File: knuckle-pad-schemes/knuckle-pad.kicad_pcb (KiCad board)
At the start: 2 copper layers, 127.6 x 115.3 mm, 67 parts, among them SW1 SW_Push, SW10 SW_Push, SW11 SW_Push, SW12 SW_Push, SW13 SW_Push, SW14 SW_Push, SW15 SW_Push, SW16 SW_Push, SW17 SW_Push, SW18 SW_Push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

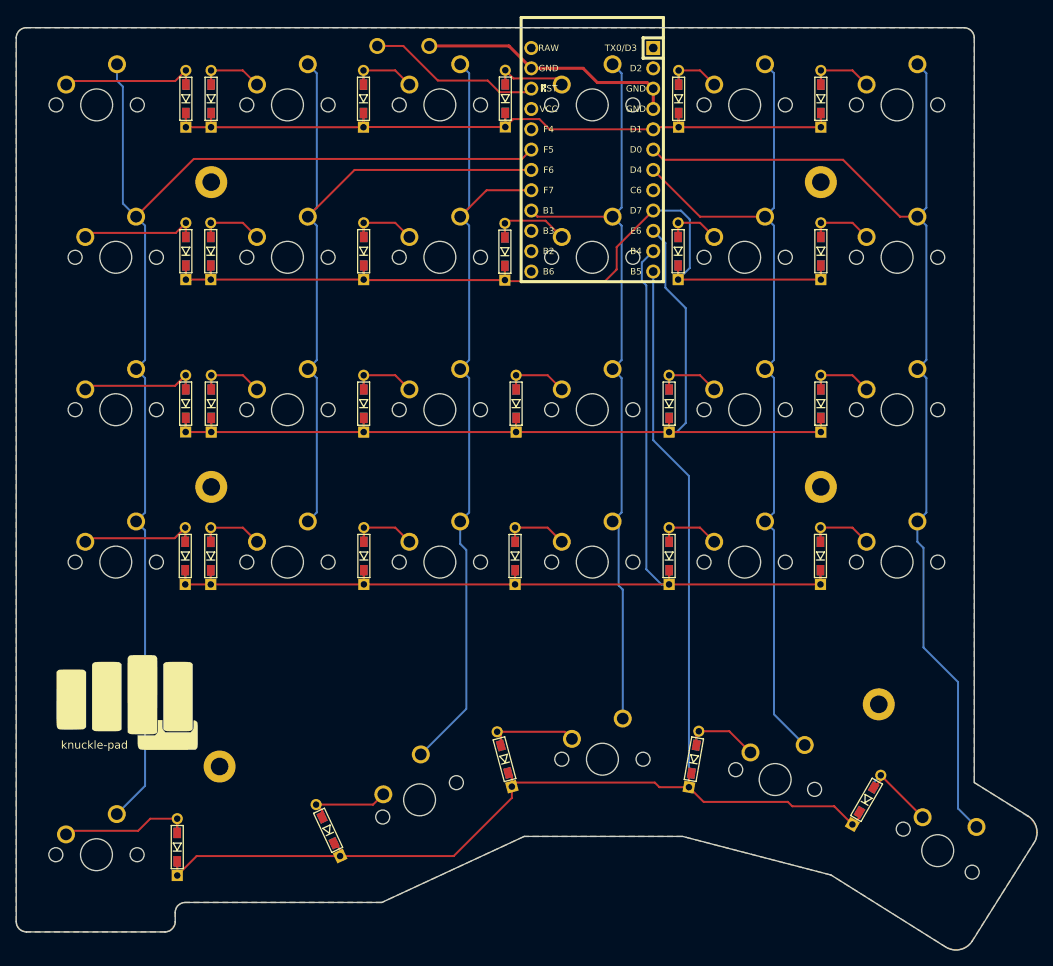
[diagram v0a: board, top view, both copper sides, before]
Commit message: changed mounting hole pos to match plate
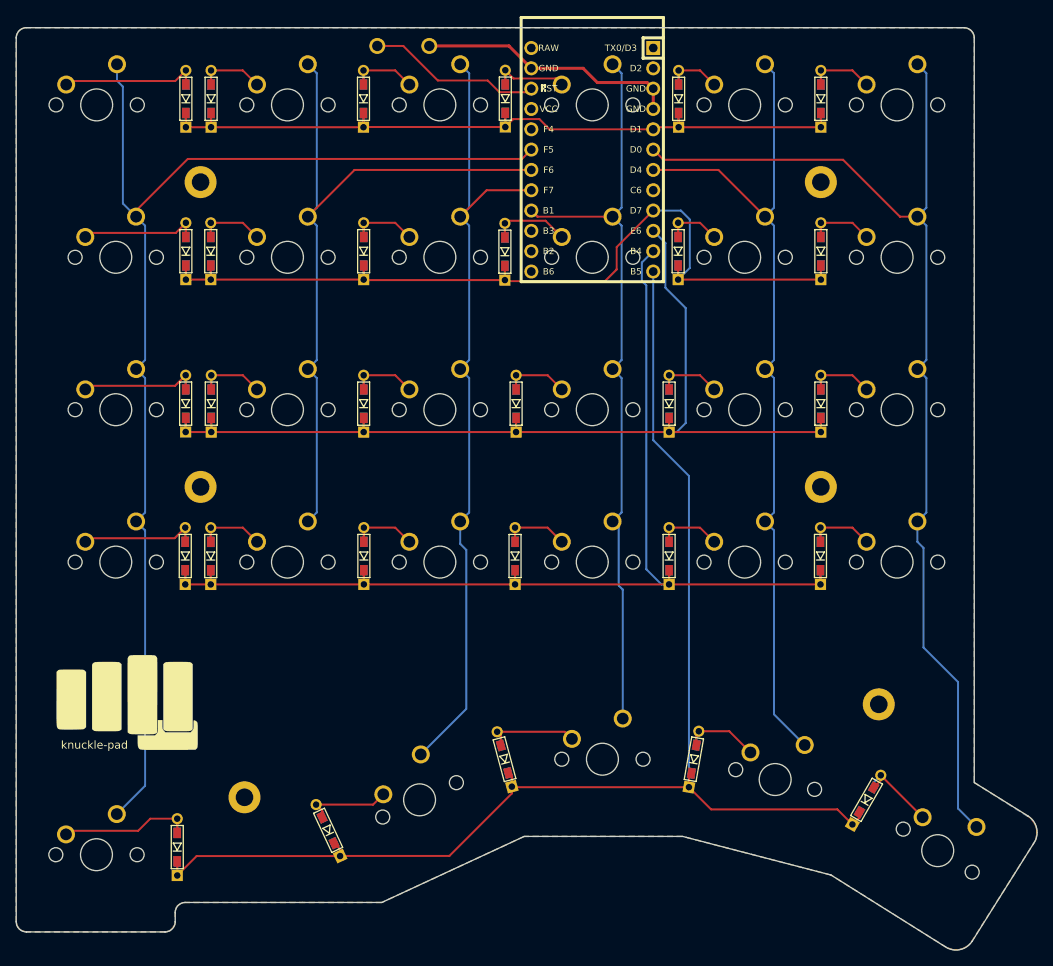
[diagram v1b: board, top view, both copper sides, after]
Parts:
- moved H3 4.95 mm to (109.4, 130.0)
- moved H2 1.33 mm to (103.9, 53.1)
- moved H4 1.33 mm to (103.9, 91.2)
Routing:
- net row4: track 177.3 -> 176.5 mm
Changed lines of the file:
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@@
     (thickness 1.6)
     (drawings 22)
-    (tracks 373)
+    (tracks 372)
     (zones 0)
     (modules 67)
@@
   )
   (module used_footprints:M2_HOLE_PCB (layer F.Cu)
-    (at 105.283 91.186)
+    (at 103.9495 91.186)
     (fp_text reference H4 (at 0 2.7) (layer F.SilkS) hide
       (effects (font (size 1 1) (thickness 0.15)))
@@
   )
   (module used_footprints:M2_HOLE_PCB (layer F.Cu)
-    (at 106.3244 126.1364)
+    (at 109.4359 129.9845)
     (fp_text reference H3 (at 0 2.7) (layer F.SilkS) hide
       (effects (font (size 1 1) (thickness 0.15)))
@@
   )
   (module used_footprints:M2_HOLE_PCB (layer F.Cu)
-    (at 105.283 53.086)
+    (at 103.9495 53.086)
     (fp_text reference H2 (at 0 2.7) (layer F.SilkS) hide
       (effects (font (size 1 1) (thickness 0.15)))
@@
   (segment (start 186.3105 132.48889) (end 185.423 133.37639) (width 0.25) (layer F.Cu) (net 13))
   (segment (start 186.3105 131.839195) (end 186.3105 132.48889) (width 0.25) (layer F.Cu) (net 13))
-  (segment (start 183.15297 131.10636) (end 177.90586 131.10636) (width 0.25) (layer F.Cu) (net 13))
-  (segment (start 185.423 133.37639) (end 183.15297 131.10636) (width 0.25) (layer F.Cu) (net 13))
-  (segment (start 177.90586 131.10636) (end 177.3555 130.556) (width 0.25) (layer F.Cu) (net 13))
-  (segment (start 166.829481 130.556) (end 164.991549 128.718068) (width 0.25) (layer F.Cu) (net 13))
-  (segment (start 177.3555 130.556) (end 166.829481 130.556) (width 0.25) (layer F.Cu) (net 13))
-  (segment (start 164.991549 128.718068) (end 161.293568 128.718068) (width 0.25) (layer F.Cu) (net 13))
-  (segment (start 161.293568 128.718068) (end 160.7185 128.143) (width 0.25) (layer F.Cu) (net 13))
-  (segment (start 143.364249 128.143) (end 142.856212 128.651037) (width 0.25) (layer F.Cu) (net 13))
-  (segment (start 160.7185 128.143) (end 143.364249 128.143) (width 0.25) (layer F.Cu) (net 13))
   (segment (start 164.991549 127.278259) (end 165.299774 126.970034) (width 0.25) (layer F.Cu) (net 13))
   (segment (start 164.991549 128.718068) (end 164.991549 127.278259) (width 0.25) (layer F.Cu) (net 13))
   (segment (start 142.856212 127.395922) (end 142.396808 126.936518) (width 0.25) (layer F.Cu) (net 13))
   (segment (start 142.856212 128.651037) (end 142.856212 127.395922) (width 0.25) (layer F.Cu) (net 13))
-  (segment (start 142.856212 128.651037) (end 142.856212 130.066788) (width 0.25) (layer F.Cu) (net 13))
-  (segment (start 135.593607 137.329393) (end 121.388295 137.329393) (width 0.25) (layer F.Cu) (net 13))
-  (segment (start 142.856212 130.066788) (end 135.593607 137.329393) (width 0.25) (layer F.Cu) (net 13))
   (segment (start 121.388295 136.470844) (end 120.638147 135.720696) (width 0.25) (layer F.Cu) (net 13))
   (segment (start 121.388295 137.329393) (end 121.388295 136.470844) (width 0.25) (layer F.Cu) (net 13))
@@
   (segment (start 164.991549 89.807549) (end 160.528 85.344) (width 0.25) (layer B.Cu) (net 13))
   (segment (start 164.991549 128.718068) (end 164.991549 89.807549) (width 0.25) (layer B.Cu) (net 13))
+  (segment (start 142.923243 128.718068) (end 142.856212 128.651037) (width 0.25) (layer F.Cu) (net 13))
+  (segment (start 164.991549 128.718068) (end 142.923243 128.718068) (width 0.25) (layer F.Cu) (net 13))
+  (segment (start 121.405288 137.3124) (end 121.388295 137.329393) (width 0.25) (layer F.Cu) (net 13))
+  (segment (start 135.0518 137.3124) (end 121.405288 137.3124) (width 0.25) (layer F.Cu) (net 13))
+  (segment (start 142.856212 129.507988) (end 135.0518 137.3124) (width 0.25) (layer F.Cu) (net 13))
+  (segment (start 142.856212 128.651037) (end 142.856212 129.507988) (width 0.25) (layer F.Cu) (net 13))
+  (segment (start 167.769281 131.4958) (end 164.991549 128.718068) (width 0.25) (layer F.Cu) (net 13))
+  (segment (start 183.54241 131.4958) (end 167.769281 131.4958) (width 0.25) (layer F.Cu) (net 13))
+  (segment (start 185.423 133.37639) (end 183.54241 131.4958) (width 0.25) (layer F.Cu) (net 13))
   (segment (start 101.0285 134.4325) (end 101.0285 132.6575) (width 0.25) (layer F.Cu) (net 14))
   (segment (start 101.0285 132.6575) (end 97.657 132.6575) (width 0.25) (layer F.Cu) (net 14))
@@
   (segment (start 95.885 95.504) (end 97.009999 96.628999) (width 0.25) (layer B.Cu) (net 39))
   (segment (start 144.1196 50.1904) (end 145.288 49.022) (width 0.25) (layer F.Cu) (net 39))
-  (segment (start 103.0986 50.1904) (end 144.1196 50.1904) (width 0.25) (layer F.Cu) (net 39))
-  (segment (start 95.885 57.404) (end 103.0986 50.1904) (width 0.25) (layer F.Cu) (net 39))
+  (segment (start 102.3493 50.1904) (end 144.1196 50.1904) (width 0.25) (layer F.Cu) (net 39))
+  (segment (start 95.885 56.6547) (end 102.3493 50.1904) (width 0.25) (layer F.Cu) (net 39))
+  (segment (start 95.885 57.404) (end 95.885 56.6547) (width 0.25) (layer F.Cu) (net 39))
   (segment (start 118.472999 56.279001) (end 117.348 57.404) (width 0.25) (layer B.Cu) (net 40))
   (segment (start 118.472999 39.478999) (end 118.472999 56.279001) (width 0.25) (layer B.Cu) (net 40))
@@
   (segment (start 175.622999 96.628999) (end 175.622999 119.608864) (width 0.25) (layer B.Cu) (net 43))
   (segment (start 174.498 95.504) (end 175.622999 96.628999) (width 0.25) (layer B.Cu) (net 43))
-  (segment (start 166.37 57.404) (end 160.528 51.562) (width 0.25) (layer F.Cu) (net 43))
-  (segment (start 174.498 57.404) (end 166.37 57.404) (width 0.25) (layer F.Cu) (net 43))
+  (segment (start 168.6687 51.562) (end 160.528 51.562) (width 0.25) (layer F.Cu) (net 43))
+  (segment (start 174.498 57.3913) (end 168.6687 51.562) (width 0.25) (layer F.Cu) (net 43))
+  (segment (start 174.498 57.404) (end 174.498 57.3913) (width 0.25) (layer F.Cu) (net 43))
   (segment (start 194.31 75.692) (end 193.548 76.454) (width 0.25) (layer B.Cu) (net 44))
   (segment (start 194.31 94.742) (end 193.548 95.504) (width 0.25) (layer B.Cu) (net 44))

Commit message: clean up
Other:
- board size 127.6 x 115.3 mm -> 127.2 x 115.3 mm
- board text added: "designed by /github.com/tileissner"
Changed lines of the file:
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@@
   (general
     (thickness 1.6)
-    (drawings 22)
+    (drawings 23)
     (tracks 372)
     (zones 0)
@@
     )
   )
-  (gr_text knuckle-pad (at 90.678 123.444) (layer F.SilkS)
-    (effects (font (size 1 1) (thickness 0.15)))
+  (gr_text "designed by /github.com/tileissner" (at 94.6912 124.64034) (layer F.SilkS)
+    (effects (font (size 0.5842 0.6477) (thickness 0.0762)))
+  )
+  (gr_arc (start 82.5754 35.052) (end 82.5754 33.782) (angle -90) (layer Edge.Cuts) (width 0.05))
+  (gr_arc (start 82.5754 145.542) (end 81.3054 145.542) (angle -90) (layer Edge.Cuts) (width 0.05))
+  (gr_text knuckle-pad (at 90.8558 123.00712) (layer F.SilkS)
+    (effects (font (size 1.0414 1.0414) (thickness 0.13335)))
   )
   (gr_arc (start 206.121001 134.365999) (end 207.391 132.334) (angle 93.53229458) (layer Edge.Cuts) (width 0.05))
   (gr_arc (start 198.374001 146.685001) (end 200.406 147.955) (angle 93.53229458) (layer Edge.Cuts) (width 0.05))
   (gr_line (start 200.66 35.052) (end 200.66 128.143) (layer Edge.Cuts) (width 0.05))
-  (gr_line (start 82.169 33.782) (end 199.39 33.782) (layer Edge.Cuts) (width 0.05))
-  (gr_line (start 80.899 145.542) (end 80.899 35.052) (layer Edge.Cuts) (width 0.05))
+  (gr_line (start 82.5754 33.782) (end 199.39 33.782) (layer Edge.Cuts) (width 0.05))
+  (gr_line (start 81.3054 145.542) (end 81.3054 35.052) (layer Edge.Cuts) (width 0.05))
   (gr_arc (start 199.39 35.052) (end 200.66 35.052) (angle -90) (layer Edge.Cuts) (width 0.05))
-  (gr_arc (start 82.169 35.052) (end 82.169 33.782) (angle -90) (layer Edge.Cuts) (width 0.05))
   (gr_line (start 102.0445 143.129) (end 116.713 143.129) (layer Edge.Cuts) (width 0.05))
   (gr_line (start 100.7745 145.542) (end 100.7745 144.399) (layer Edge.Cuts) (width 0.05))
-  (gr_line (start 82.169 146.812) (end 99.5045 146.812) (layer Edge.Cuts) (width 0.05))
+  (gr_line (start 82.5754 146.812) (end 99.5045 146.812) (layer Edge.Cuts) (width 0.05))
   (gr_arc (start 102.0445 144.399) (end 102.0445 143.129) (angle -90) (layer Edge.Cuts) (width 0.05))
   (gr_arc (start 99.5045 145.542) (end 99.5045 146.812) (angle -90) (layer Edge.Cuts) (width 0.05))
   (gr_line (start 116.713 143.129) (end 126.619 143.129) (layer Edge.Cuts) (width 0.05))
-  (gr_arc (start 82.169 145.542) (end 80.899 145.542) (angle -90) (layer Edge.Cuts) (width 0.05))
   (gr_line (start 207.391 132.334) (end 200.66 128.143) (layer Edge.Cuts) (width 0.05))
   (gr_line (start 126.619 143.129) (end 126.873 143.002) (layer Edge.Cuts) (width 0.05))
@@
         (xy 144.399 134.874) (xy 126.619 143.129) (xy 101.7905 143.129) (xy 101.346 143.3195) (xy 100.965 143.637)
         (xy 100.7745 144.2085) (xy 100.7745 145.6055) (xy 100.711 145.923) (xy 100.457 146.304) (xy 100.076 146.685)
-        (xy 99.568 146.812) (xy 82.169 146.812) (xy 81.661 146.685) (xy 81.28 146.431) (xy 81.026 146.05)
-        (xy 80.899 145.542) (xy 80.899 35.0012) (xy 80.9752 34.6456) (xy 81.2292 34.1884) (xy 81.5848 33.9344)
-        (xy 82.042 33.782) (xy 199.2884 33.782)
+        (xy 99.568 146.812) (xy 82.7278 146.812) (xy 82.3214 146.7866) (xy 81.7118 146.4818) (xy 81.4578 146.1516)
+        (xy 81.3054 145.542) (xy 81.3054 35.0266) (xy 81.3816 34.6456) (xy 81.6102 34.2138) (xy 81.8896 33.9852)
+        (xy 82.5246 33.782) (xy 199.2884 33.782)
       )
     )
@@
         (xy 126.619 143.129) (xy 101.7905 143.129) (xy 101.346 143.3195) (xy 100.965 143.637) (xy 100.7745 144.2085)
         (xy 100.7745 145.6055) (xy 100.711 145.923) (xy 100.457 146.304) (xy 100.076 146.685) (xy 99.568 146.812)
-        (xy 82.169 146.812) (xy 81.661 146.685) (xy 81.28 146.431) (xy 81.026 146.05) (xy 80.899 145.542)
-        (xy 80.899 35.0012) (xy 80.9752 34.6456) (xy 81.2292 34.1884) (xy 81.5848 33.9344) (xy 82.042 33.782)
+        (xy 82.7278 146.812) (xy 82.3214 146.7866) (xy 81.7118 146.4818) (xy 81.4578 146.1516) (xy 81.3054 145.53565)
+        (xy 81.3054 35.0266) (xy 81.3816 34.6456) (xy 81.6102 34.2138) (xy 81.8896 33.9852) (xy 82.5246 33.782)
         (xy 199.2884 33.782)
       )
